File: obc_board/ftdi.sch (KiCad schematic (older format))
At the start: 20 parts, among them J16 Conn_01x04_Female, U15 AP2127N-3.3, U16 FT4232H-56Q-REEL, Y4 12MHz

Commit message: layout done
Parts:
- renumbered R111 to R105, R112 to R106, R113 to R107
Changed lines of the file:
@@
 $EndDescr
 $Comp
-L Device:R R111
+L Device:R R105
 U 1 1 5F3FD422
 P 4250 2900
-F 0 "R111" V 4043 2900 50  0000 C CNN
+F 0 "R105" V 4043 2900 50  0000 C CNN
 F 1 "1k" V 4134 2900 50  0000 C CNN
 F 2 "Resistor_SMD:R_0402_1005Metric" V 4180 2900 50  0001 C CNN
@@
 $EndComp
 $Comp
-L Device:R R113
+L Device:R R107
 U 1 1 5F3FF77C
 P 5000 3550
-F 0 "R113" H 5070 3596 50  0000 L CNN
+F 0 "R107" H 5070 3596 50  0000 L CNN
 F 1 "12k" H 5070 3505 50  0000 L CNN
 F 2 "Resistor_SMD:R_0201_0603Metric" V 4930 3550 50  0001 C CNN
@@
 OSC_OUT
 $Comp
-L Device:R R112
+L Device:R R106
 U 1 1 5F3FDD47
 P 4800 3200
-F 0 "R112" H 4870 3246 50  0000 L CNN
+F 0 "R106" H 4870 3246 50  0000 L CNN
 F 1 "100k" H 4870 3155 50  0000 L CNN
 F 2 "Resistor_SMD:R_0402_1005Metric" V 4730 3200 50  0001 C CNN

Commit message: relayout
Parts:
- renumbered C44 to C39, C45 to C40, C46 to C41, C47 to C42, C48 to C43, C49 to C44, C50 to C45, C51 to C46, C52 to C47, C53 to C48, C54 to C49, C55 to C50, J16 to J15, R105 to R112, R106 to R113, R107 to R114, U15 to U17, U16 to U18, Y4 to Y2
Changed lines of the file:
@@
 $Descr A4 11693 8268
 encoding utf-8
-Sheet 8 8
+Sheet 7 8
 Title ""
 Date ""
@@
 $EndDescr
 $Comp
-L Device:R R105
+L Device:R R112
 U 1 1 5F3FD422
 P 4250 2900
-F 0 "R105" V 4043 2900 50  0000 C CNN
+F 0 "R112" V 4043 2900 50  0000 C CNN
 F 1 "1k" V 4134 2900 50  0000 C CNN
 F 2 "Resistor_SMD:R_0402_1005Metric" V 4180 2900 50  0001 C CNN
@@
 $EndComp
 $Comp
-L Device:R R107
+L Device:R R114
 U 1 1 5F3FF77C
 P 5000 3550
-F 0 "R107" H 5070 3596 50  0000 L CNN
+F 0 "R114" H 5070 3596 50  0000 L CNN
 F 1 "12k" H 5070 3505 50  0000 L CNN
 F 2 "Resistor_SMD:R_0201_0603Metric" V 4930 3550 50  0001 C CNN
@@
 GND
 $Comp
-L Connector:Conn_01x04_Female J16
+L Connector:Conn_01x04_Female J15
 U 1 1 5F401059
 P 2700 3850
-F 0 "J16" V 2638 3562 50  0000 R CNN
+F 0 "J15" V 2638 3562 50  0000 R CNN
 F 1 "Conn_01x04_Female" V 2547 3562 50  0000 R CNN
 F 2 "Connector_Molex:Molex_PicoBlade_53261-0471_1x04-1MP_P1.25mm_Horizontal" H 2700 3850 50  0001 C CNN
@@
 $EndComp
 $Comp
-L Regulator_Linear:AP2127N-3.3 U15
+L Regulator_Linear:AP2127N-3.3 U17
 U 1 1 5F4056A6
 P 3950 1650
-F 0 "U15" H 3950 1892 50  0000 C CNN
+F 0 "U17" H 3950 1892 50  0000 C CNN
 F 1 "AP2127N-3.3" H 3950 1801 50  0000 C CNN
 F 2 "Package_TO_SOT_SMD:SOT-23" H 3950 1875 50  0001 C CIN
@@
 GND
 $Comp
-L Device:C C44
+L Device:C C39
 U 1 1 5F40A5AF
 P 3300 1850
-F 0 "C44" H 3415 1896 50  0000 L CNN
+F 0 "C39" H 3415 1896 50  0000 L CNN
 F 1 "100n" H 3415 1805 50  0000 L CNN
 F 2 "Capacitor_SMD:C_0402_1005Metric" H 3338 1700 50  0001 C CNN
@@
 	3300 1650 3650 1650
 $Comp
-L Device:C C47
+L Device:C C42
 U 1 1 5F40C428
 P 4450 1850
-F 0 "C47" H 4565 1896 50  0000 L CNN
+F 0 "C42" H 4565 1896 50  0000 L CNN
 F 1 "100n" H 4565 1805 50  0000 L CNN
 F 2 "Capacitor_SMD:C_0402_1005Metric" H 4488 1700 50  0001 C CNN
@@
 3V3
 $Comp
-L Device:C C49
+L Device:C C44
 U 1 1 5F41601C
 P 7950 3400
-F 0 "C49" H 8065 3446 50  0000 L CNN
+F 0 "C44" H 8065 3446 50  0000 L CNN
 F 1 "100n" H 8065 3355 50  0000 L CNN
 F 2 "Capacitor_SMD:C_0402_1005Metric" H 7988 3250 50  0001 C CNN
@@
 	5100 1650 5300 1650
 $Comp
-L Device:C C48
+L Device:C C43
 U 1 1 5F4224A6
 P 5300 1850
-F 0 "C48" H 5415 1896 50  0000 L CNN
+F 0 "C43" H 5415 1896 50  0000 L CNN
 F 1 "1u" H 5415 1805 50  0000 L CNN
 F 2 "Capacitor_SMD:C_0603_1608Metric" H 5338 1700 50  0001 C CNN
@@
 	10200 2500 10200 2450
 $Comp
-L Device:C C55
+L Device:C C50
 U 1 1 5F41BF8B
 P 10200 2650
-F 0 "C55" H 10315 2696 50  0000 L CNN
+F 0 "C50" H 10315 2696 50  0000 L CNN
 F 1 "100n" H 10315 2605 50  0000 L CNN
 F 2 "Capacitor_SMD:C_0402_1005Metric" H 10238 2500 50  0001 C CNN
@@
 GND
 $Comp
-L Device:C C53
+L Device:C C48
 U 1 1 5F41BF81
 P 9650 2650
-F 0 "C53" H 9765 2696 50  0000 L CNN
+F 0 "C48" H 9765 2696 50  0000 L CNN
 F 1 "100n" H 9765 2605 50  0000 L CNN
 F 2 "Capacitor_SMD:C_0402_1005Metric" H 9688 2500 50  0001 C CNN
@@
 	10200 1700 10200 1650
 $Comp
-L Device:C C54
+L Device:C C49
 U 1 1 5F41916C
 P 10200 1850
-F 0 "C54" H 10315 1896 50  0000 L CNN
+F 0 "C49" H 10315 1896 50  0000 L CNN
 F 1 "100n" H 10315 1805 50  0000 L CNN
 F 2 "Capacitor_SMD:C_0402_1005Metric" H 10238 1700 50  0001 C CNN
@@
 	9650 1700 9650 1650
 $Comp
-L Device:C C52
+L Device:C C47
 U 1 1 5F418802
 P 9650 1850
-F 0 "C52" H 9765 1896 50  0000 L CNN
+F 0 "C47" H 9765 1896 50  0000 L CNN
 F 1 "100n" H 9765 1805 50  0000 L CNN
 F 2 "Capacitor_SMD:C_0402_1005Metric" H 9688 1700 50  0001 C CNN
@@
 	9100 1700 9100 1650
 $Comp
-L Device:C C51
+L Device:C C46
 U 1 1 5F418102
 P 9100 1850
-F 0 "C51" H 9215 1896 50  0000 L CNN
+F 0 "C46" H 9215 1896 50  0000 L CNN
 F 1 "100n" H 9215 1805 50  0000 L CNN
 F 2 "Capacitor_SMD:C_0402_1005Metric" H 9138 1700 50  0001 C CNN
@@
 GND
 $Comp
-L Device:C C50
+L Device:C C45
 U 1 1 5F417430
 P 8550 1850
-F 0 "C50" H 8665 1896 50  0000 L CNN
+F 0 "C45" H 8665 1896 50  0000 L CNN
 F 1 "100n" H 8665 1805 50  0000 L CNN
 F 2 "Capacitor_SMD:C_0402_1005Metric" H 8588 1700 50  0001 C CNN
@@
 OSC_OUT
 $Comp
-L Device:R R106
+L Device:R R113
 U 1 1 5F3FDD47
 P 4800 3200
-F 0 "R106" H 4870 3246 50  0000 L CNN
+F 0 "R113" H 4870 3246 50  0000 L CNN
 F 1 "100k" H 4870 3155 50  0000 L CNN
 F 2 "Resistor_SMD:R_0402_1005Metric" V 4730 3200 50  0001 C CNN
@@
 	4400 2900 4800 2900
 $Comp
-L cubesat_obc_lib:FT4232H-56Q-REEL U16
+L cubesat_obc_lib:FT4232H-56Q-REEL U18
 U 1 1 5F3FC591
 P 6500 4600
-F 0 "U16" H 6500 6765 50  0000 C CNN
+F 0 "U18" H 6500 6765 50  0000 C CNN
 F 1 "FT4232H-56Q-REEL" H 6500 6674 50  0000 C CNN
 F 2 "cubesat_obc:QFN50P800X800X100-57N" H 6500 4600 50  0001 L BNN
@@
 	4800 2900 5600 2900
 $Comp
-L Device:Crystal Y4
+L Device:Crystal Y2
 U 1 1 5F4368EE
 P 3250 4900
-F 0 "Y4" V 3204 5031 50  0000 L CNN
+F 0 "Y2" V 3204 5031 50  0000 L CNN
 F 1 "12MHz" V 3295 5031 50  0000 L CNN
 F 2 "Crystal:Crystal_SMD_5032-4Pin_5.0x3.2mm" H 3250 4900 50  0001 C CNN
@@
 $EndComp
 $Comp
-L Device:C C45
+L Device:C C40
 U 1 1 5F4371A6
 P 3750 4700
-F 0 "C45" V 4002 4700 50  0000 C CNN
+F 0 "C40" V 4002 4700 50  0000 C CNN
 F 1 "20p" V 3911 4700 50  0000 C CNN
 F 2 "Capacitor_SMD:C_0201_0603Metric" H 3788 4550 50  0001 C CNN
@@
 	3250 5100 3000 5100
 $Comp
-L Device:C C46
+L Device:C C41
 U 1 1 5F43B977
 P 3750 5100
-F 0 "C46" V 3498 5100 50  0000 C CNN
+F 0 "C41" V 3498 5100 50  0000 C CNN
 F 1 "20p" V 3589 5100 50  0000 C CNN
 F 2 "Capacitor_SMD:C_0201_0603Metric" H 3788 4950 50  0001 C CNN

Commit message: modify planes
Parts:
- renumbered J15 to USB0
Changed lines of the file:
@@
 $Descr A4 11693 8268
 encoding utf-8
-Sheet 7 8
+Sheet 7 9
 Title ""
 Date ""
@@
 GND
 $Comp
-L Connector:Conn_01x04_Female J15
+L Connector:Conn_01x04_Female USB0
 U 1 1 5F401059
 P 2700 3850
-F 0 "J15" V 2638 3562 50  0000 R CNN
+F 0 "USB0" V 2638 3562 50  0000 R CNN
 F 1 "Conn_01x04_Female" V 2547 3562 50  0000 R CNN
 F 2 "Connector_Molex:Molex_PicoBlade_53261-0471_1x04-1MP_P1.25mm_Horizontal" H 2700 3850 50  0001 C CNN

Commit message: added h bridge and magnetometers
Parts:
- R113: Digikey Part Number 311-10.0KLRCT-ND -> YAG2307CT-ND
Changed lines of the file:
@@
 $Descr A4 11693 8268
 encoding utf-8
-Sheet 7 9
+Sheet 7 10
 Title ""
 Date ""
@@
 F 1 "1k" V 4134 2900 50  0000 C CNN
 F 2 "Resistor_SMD:R_0402_1005Metric" V 4180 2900 50  0001 C CNN
-F 3 "https://www.yageo.com/upload/media/product/productsearch/datasheet/rchip/PYu-RC_Group_51_RoHS_L_11.pdf~" H 4250 2900 50  0001 C CNN
+F 3 "https://www.yageo.com/upload/media/product/productsearch/datasheet/rchip/PYu-RC_Group_51_RoHS_L_11.pdf" H 4250 2900 50  0001 C CNN
 F 4 "311-1.00KLRCT-ND" H 4250 2900 50  0001 C CNN "Digikey Part Number"
 	1    4250 2900
@@
 F 1 "100k" H 4870 3155 50  0000 L CNN
 F 2 "Resistor_SMD:R_0402_1005Metric" V 4730 3200 50  0001 C CNN
-F 3 "https://www.yageo.com/upload/media/product/productsearch/datasheet/rchip/PYu-RC_Group_51_RoHS_L_11.pdf" H 4800 3200 50  0001 C CNN
-F 4 "311-10.0KLRCT-ND" H 4800 3200 50  0001 C CNN "Digikey Part Number"
+F 3 "https://www.yageo.com/upload/media/product/productsearch/datasheet/rchip/PYu-RC_Group_51_RoHS_L_11.pdfhttps://www.yageo.com/upload/media/product/productsearch/datasheet/rchip/PYu-RT_1-to-0.01_RoHS_L_12.pdf" H 4800 3200 50  0001 C CNN
+F 4 "YAG2307CT-ND" H 4800 3200 50  0001 C CNN "Digikey Part Number"
 	1    4800 3200
 	1    0    0    -1

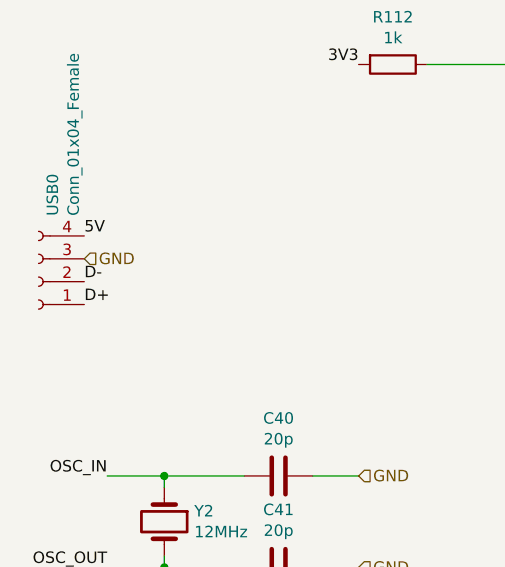
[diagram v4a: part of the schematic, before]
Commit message: reduce via
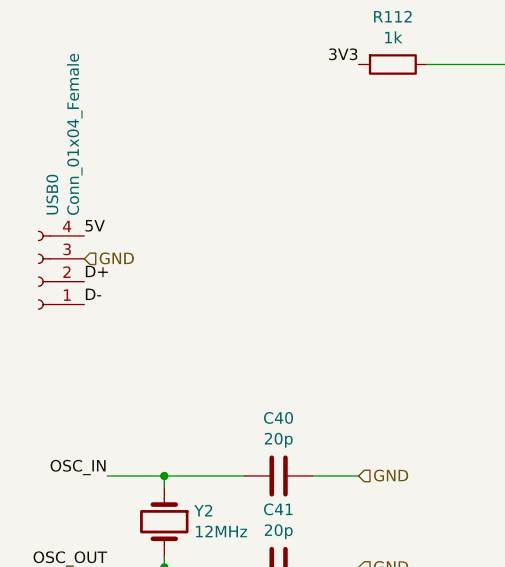
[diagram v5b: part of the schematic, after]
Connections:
- net D+: now also USB0.2 (Pin_2); no longer USB0.1 (Pin_1)
- net D-: now also USB0.1 (Pin_1); no longer USB0.2 (Pin_2)
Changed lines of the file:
@@
 Text Label 8350 1650 2    50   ~ 0
 3V3
+Text Label 2900 3850 0    50   ~ 0
+D+
 Text Label 2900 3950 0    50   ~ 0
-D+
-Text Label 2900 3850 0    50   ~ 0
 D-
 Text HLabel 5600 5200 0    50   Input ~ 0
